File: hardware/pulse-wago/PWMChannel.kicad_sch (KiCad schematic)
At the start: 6 parts, among them J201 WAGO-2065, J202 WAGO-2065, Q201 BSC010N04LS

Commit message: Update library
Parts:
- C201: footprint Capacitor_SMD:C_0603_1608Metric -> V2_Capacitor_SMD:C_0603; symbol Device:C_Small -> V2_Device:C_0603_0u1; Manufacturer (none) -> TDK; Mouser (none) -> 810-CGA3E2X7R1H104MA; Product (none) -> CGA3E2X7R1H104M080AA; Rating (none) -> 50V
- D201: footprint Diode_SMD:D_SOD-123F -> V2_Diode_SMD:D_SOD-123F; Manufacturer (none) -> onsemi; Mouser (none) -> 512-S310FA; Product (none) -> S310FA
- D202: LCSC (none) -> C965555; Manufacturer (none) -> Worldsemi; Product (none) -> WS2812B-2020
- J201, J202: value WAGO-2065 -> WAGO 2601-1101; Manufacturer (none) -> WAGO; Product (none) -> 2601-1101
- Q201: Manufacturer (none) -> Infineon Technologies; Mouser (none) -> 726-BSC010N04LS; Polarity (none) -> N; Product (none) -> BSC010N04LS; Rating (none) -> 40V
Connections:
- net +24V renamed +28V
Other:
- moved on the sheet: D201

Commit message: Update Library
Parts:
- C201: symbol V2_Device:C_0603_0u1 -> V2_Capacitor:0603_0u1

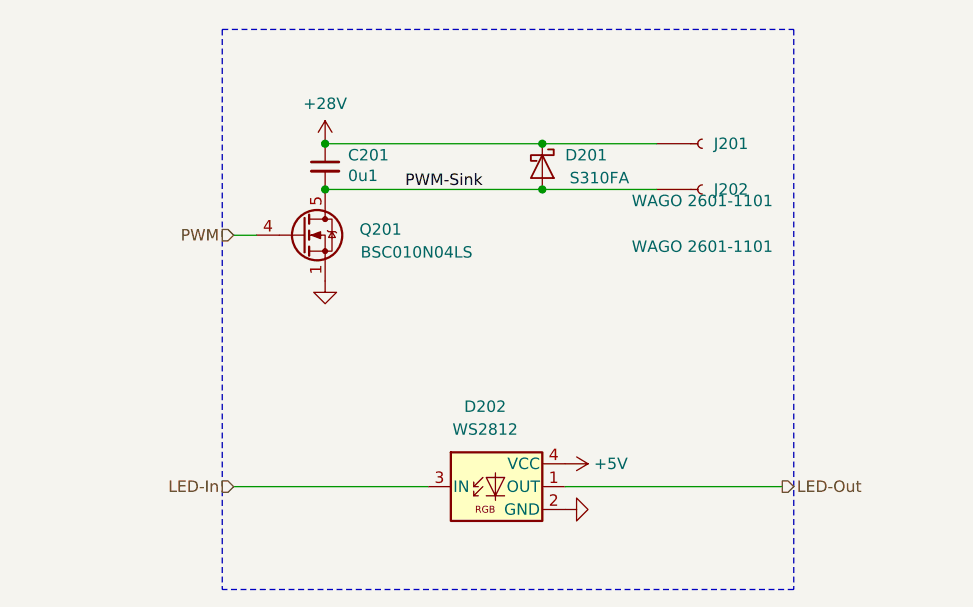
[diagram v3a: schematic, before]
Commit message: Replace diode
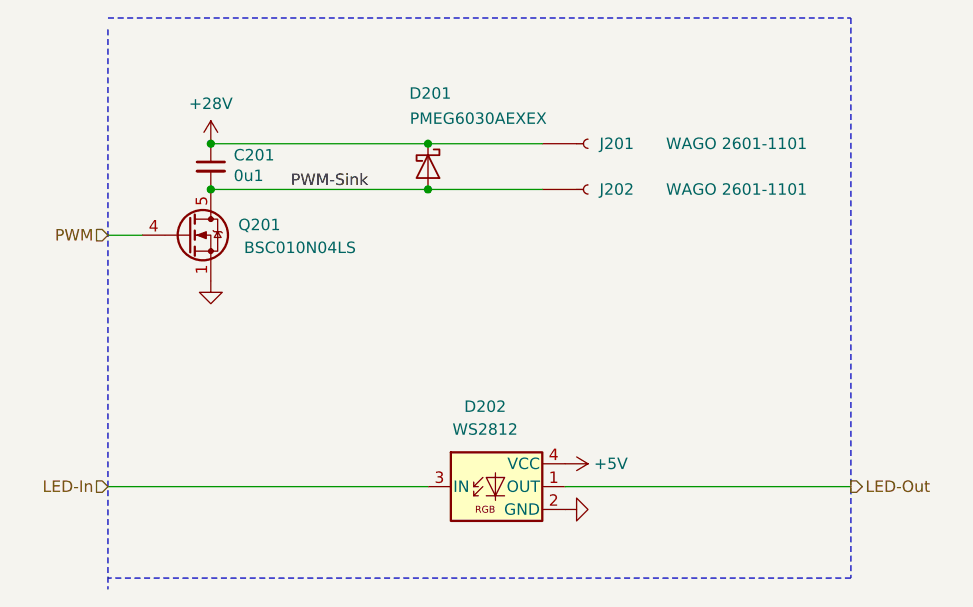
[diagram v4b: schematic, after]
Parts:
- D201: value S310FA -> PMEG6030AEXEX; footprint V2_Diode_SMD:D_SOD-123F -> V2_Diode_SMD:D_SOD-123HP; symbol V2_Diode:S310FA -> V2_Diode:PMEG6030AEXEX; Manufacturer onsemi -> Nexperia; Mouser 512-S310FA -> 771-PMEG6030AEXEX; Product S310FA -> PMEG6030AEXEX
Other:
- moved on the sheet: C201, D201, J201, J202, Q201

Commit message: Update ESD suppressor
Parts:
- D201: Rating (none) -> 60V
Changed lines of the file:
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@@
+			)
+		)
+		(property "Rating" "60V"
+			(at 127 88.9 0)
+			(effects
+				(font
+					(size 1.27 1.27)
+				)
+				(hide yes)
 			)
 		)

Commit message: Replace diode
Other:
- title: Solenoid Channel -> V2 pulse WAGO

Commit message: Update
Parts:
- C201: Id (none) -> Capacitor:${SYMBOL_NAME}
- D201: Id (none) -> Diode:${SYMBOL_NAME}
- D202: Id (none) -> LED:${SYMBOL_NAME}; Rating (none) -> 15mA
- J201, J202: Id (none) -> WAGO:${SYMBOL_NAME}; Rating (none) -> 17.5A
- Q201: Id (none) -> MOSFET:${SYMBOL_NAME}
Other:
- company: Power MOSFET + RGB LED -> Versio Duo

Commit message: Good Bye Imperial
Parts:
- C201: footprint V2_Capacitor_SMD:C_0603 -> V2_Capacitor_SMD:C_1608; symbol V2_Capacitor:0603_0u1 -> V2_Capacitor:1608_0u1
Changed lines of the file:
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@@
 	)
 	(symbol
-		(lib_id "V2_Capacitor:0603_0u1")
+		(lib_id "V2_Capacitor:1608_0u1")
 		(at 120.65 88.9 0)
 		(unit 1)
@@
 			)
 		)
-		(property "Footprint" "V2_Capacitor_SMD:C_0603"
+		(property "Footprint" "V2_Capacitor_SMD:C_1608"
 			(at 120.65 105.918 0)
 			(hide yes)
